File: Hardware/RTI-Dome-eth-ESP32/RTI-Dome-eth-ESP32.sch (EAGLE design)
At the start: 101 parts, among them IC1 REG1117FA-5.0_500, IC2 24LC64T-I/SN, IC8 REG1117-3.3V, J2 XT60PW-M, T1 MMBT3904LT1, T2 MMBT3904LT1, T3 MMBT3904LT1, U1 W5500, U2 ESP32-DevKitC ESP32-WROOM-32U, X9 J1011F01PNL

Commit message: Use switching regulator for the 5v. Can take from 8V to 40V in.
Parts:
- removed C2: 100uF, samacsys:MAL215099804E3""
- removed C27, C28, C3: 10uF, rcl:C-EUC0603
- removed IC1: REG1117FA-5.0_500, REG1117FA-5.0_500:REG1117FA-5.0_500
- removed X11: (no value), rti:AK500/2
- added C25, C26: 180uF, samacsys:EEE-FNE181XUP
- added C29, C30, C31: 15uF 50V, samacsys:865080643007
- added C7: 1nF, rcl:C-EUC0805
- added C8: 10nF, rcl:C-EUC0805
- added C9: 470nF, rcl:C-EUC1206
- added D2: VSSAF5L45-M3_6A, samacsys:VSSAF5L45-M3_6A
- added IC3: LM2679SD-5.0_NOPB, samacsys:LM2679SD-5.0_NOPB
- added L1: SRP1038CC-220M, samacsys:SRP1038CC-220M
- added R11: 5.6K, rcl:R-EU_R0603
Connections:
- new net 5V_SW: C8.1, D2.K, IC3.SWITCH_OUTPUT_1, IC3.SWITCH_OUTPUT_2, IC3.SWITCH_OUTPUT_3, L1.1
- new net CB: C8.2, IC3.CB
- new net N$1: IC3.CURRENT_ADJUST, R11.1
- new net N$4: C7.2, IC3.SS
- net +12V: now also C29.+, C30.+, C31.+, C9.2, IC3.INPUT_1, IC3.INPUT_2; no longer C2.+, C27.1, C3.1, IC1.VIN, X11-2.KL
- net GND: now also C25.-, C26.-, C29.-, C30.-, C31.-, C7.1, C9.1, D2.A, IC3.EP, IC3.GND, R11.2; no longer C2.-, C27.2, C28.2, C3.2, IC1.GND, X11-1.KL
- net VCC: now also C25.+, C26.+, IC3.FB, L1.2; no longer C28.1, IC1.VOUT_1, IC1.VOUT_2
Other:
- moved on the sheet: JP1, U2

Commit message: Switch IO port to Wurth ones.
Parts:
- removed R10, R2, R6, R7, R8: 100K 0.1%, rcl:R-EU_R0603
- removed X1, X12, X3, X8: (no value), rti:AK500/2
- removed X10, X2, X4, X5, X6, X7: (no value), rti:AK500/3
- added J1, J3, J4, J6, J7: 691313510003, samacsys:691313510003
- added J10, J11, J12, J8, J9: 691313510002, samacsys:691313510002
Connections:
- removed net N$2: R7.2, R8.1
- removed net N$3: R10.1, R8.2
- removed net N$5: R2.2, R7.1
- net +12V: now also J7.1; no longer R10.2, X5-1.KL
- net AT_PARK_PIN-IN_EXT: now also J11.2; no longer X12-2.KL
- net BUTTON_EAST_OPEN-IN_EXT: now also J6.2; no longer X4-2.KL
- net BUTTON_WEST_CLOSE-IN_EXT: now also J6.3; no longer X4-3.KL
- net DIR_5V_OUT: now also J3.2; no longer X10-2.KL
- net EN_5V_OUT: now also J4.2; no longer X2-2.KL
- net GND: now also J1.1, J11.1, J3.1, J4.1, J6.1, J7.3, J8.1, J9.1; no longer R6.1, X1-1.KL, X10-1.KL, X12-1.KL, X2-1.KL, X3-1.KL, X4-1.KL, X5-3.KL, X6-1.KL, X7-1.KL
- net HOME_SHUTTER_CLOSED-IN_EXT: now also J8.2; no longer X1-2.KL
- net RG-11-IN_EXT: now also J7.2; no longer X5-2.KL
- net SHUTTER_OPENED-IN_EXT: now also J9.2; no longer X3-2.KL
- net SPARE1-IN_EXT: now also J10.1; no longer X8-1.KL
- net SPARE2-IN_EXT: now also J10.2; no longer X8-2.KL
- net SPARE_OUT1_5V: now also J12.2; no longer X7-3.KL
- net SPARE_OUT2_5V: now also J12.1; no longer X7-2.KL
- net STEP_5V_OUT: now also J1.2; no longer X6-2.KL
- net VCC: now also J1.3, J3.3, J4.3; no longer X10-3.KL, X2-3.KL, X6-3.KL
- net VPIN: no longer R2.1, R6.2
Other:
- moved on the sheet: J2

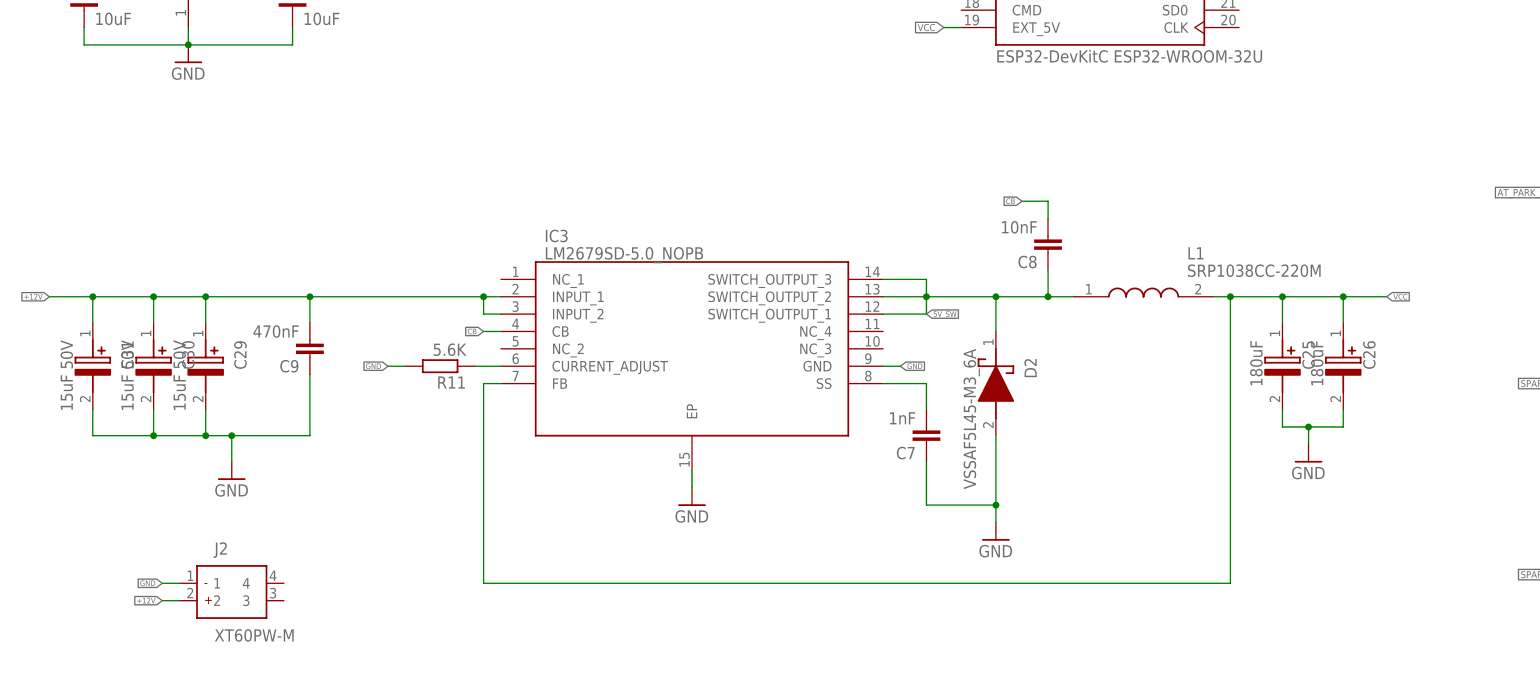
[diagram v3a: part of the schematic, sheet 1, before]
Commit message: Change the 5V regulator on the rotatyor esp32 board.
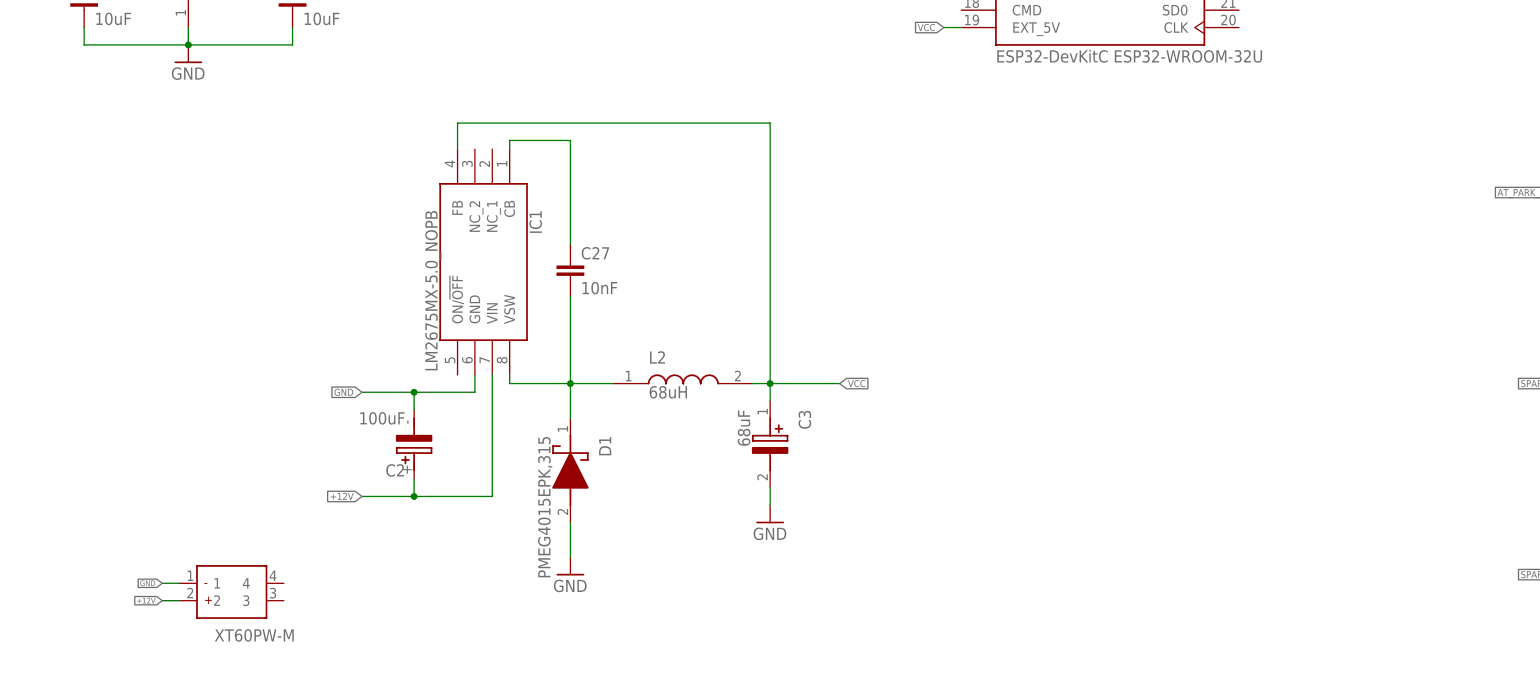
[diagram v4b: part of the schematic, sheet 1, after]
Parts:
- removed C25, C26: 180uF, samacsys:EEE-FNE181XUP
- removed C29, C30, C31: 15uF 50V, samacsys:865080643007
- removed C7: 1nF, rcl:C-EUC0805
- removed C8: 10nF, rcl:C-EUC0805
- removed C9: 470nF, rcl:C-EUC1206
- removed D2: VSSAF5L45-M3_6A, samacsys:VSSAF5L45-M3_6A
- removed IC3: LM2679SD-5.0_NOPB, samacsys:LM2679SD-5.0_NOPB
- removed L1: SRP1038CC-220M, samacsys:SRP1038CC-220M
- removed R11: 5.6K, rcl:R-EU_R0603
- added C2: 100uF, samacsys:MAL215099804E3""
- added C27: 10nF, rcl:C-EUC0805
- added C3: 68uF, samacsys:EEE-FP1C680AL
- added D1: PMEG4015EPK,315, samacsys:PMEG4015EPK,315
- added IC1: LM2675MX-5.0_NOPB, samacsys:LM2675MX-5.0_NOPB
- added L2: 68uH, samacsys:784777470
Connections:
- removed net 5V_SW: C8.1, D2.K, IC3.SWITCH_OUTPUT_1, IC3.SWITCH_OUTPUT_2, IC3.SWITCH_OUTPUT_3, L1.1
- removed net CB: C8.2, IC3.CB
- removed net N$1: IC3.CURRENT_ADJUST, R11.1
- removed net N$4: C7.2, IC3.SS
- new net N$2: C27.1, IC1.CB
- new net SWV: C27.2, D1.K, IC1.VSW, L2.1
- net +12V: now also C2.+, IC1.VIN; no longer C29.+, C30.+, C31.+, C9.2, IC3.INPUT_1, IC3.INPUT_2
- net GND: now also C2.-, C3.-, D1.A, IC1.GND; no longer C25.-, C26.-, C29.-, C30.-, C31.-, C7.1, C9.1, D2.A, IC3.EP, IC3.GND, R11.2
- net VCC: now also C3.+, IC1.FB, L2.2; no longer C25.+, C26.+, IC3.FB, L1.2

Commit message: Fix components orientation in the library to match JLCPCB
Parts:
- C2: MPN (none) -> C249838
- IC2: device Microchip_By_element14_Batch_1:24LC64T-I/SN -> rti:24LC64T-I/SN
- L2: value 68uH -> 47uH; MPN (none) -> 784777470
- R23: value 10 1% -> 10.0 1%; MPN RT0805FRE1310RL -> C881123
- U2: value ESP32-DevKitC ESP32-WROOM-32U -> ESP32-DevKitC-32UE
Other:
- moved on the sheet: C2, C27, C3, D1, IC1, L2

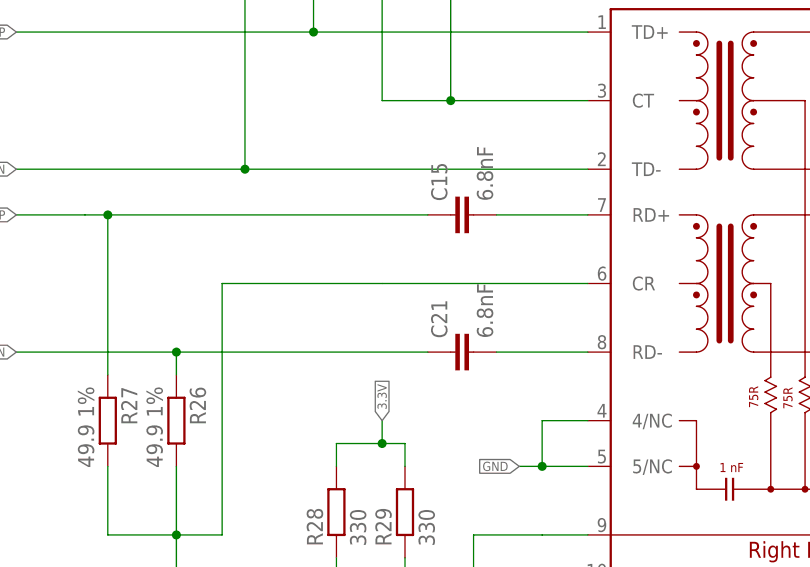
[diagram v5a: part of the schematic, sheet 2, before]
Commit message: Re-adding the domeClient.stop();
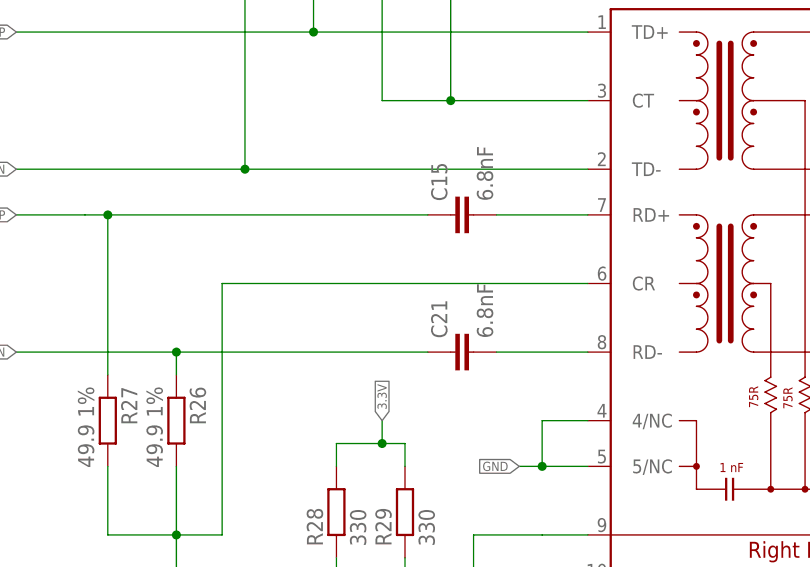
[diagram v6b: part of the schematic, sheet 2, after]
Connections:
- net N$10 renamed L_LED+
- net N$11 renamed RD+
- net N$12 renamed RD-
- net N$13 renamed CT
- net N$7 renamed CR
- net N$8 renamed R_LED+
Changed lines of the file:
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@@
 <part name="FRAME1" library="frames" library_urn="urn:adsk.eagle:library:229" deviceset="DINA3_L" device=""/>
 <part name="GND7" library="supply1" library_urn="urn:adsk.eagle:library:371" deviceset="GND" device=""/>
-<part name="U1" library="W5500" library_urn="urn:adsk.eagle:library:37501005" deviceset="W5500" device="" package3d_urn="urn:adsk.eagle:package:37501008/3" value="W5500">
+<part name="U1" library="W5500" library_urn="urn:adsk.eagle:library:37501005" deviceset="W5500" device="" package3d_urn="urn:adsk.eagle:package:37501008/4" value="W5500">
 <attribute name="MPN" value="W5500"/>
 </part>
@@
 <part name="GND16" library="supply1" library_urn="urn:adsk.eagle:library:371" deviceset="GND" device=""/>
 <part name="J2" library="samacsys" library_urn="urn:adsk.eagle:library:37256869" deviceset="XT60PW-M" device="" package3d_urn="urn:adsk.eagle:package:37256940/7"/>
-<part name="IC2" library="rti" library_urn="urn:adsk.eagle:library:37256580" deviceset="24LC64T-I/SN" device="" package3d_urn="urn:adsk.eagle:package:37894665/5"/>
+<part name="IC2" library="rti" library_urn="urn:adsk.eagle:library:37256580" deviceset="24LC64T-I/SN" device="" package3d_urn="urn:adsk.eagle:package:37894665/6"/>
 <part name="GND21" library="supply1" library_urn="urn:adsk.eagle:library:371" deviceset="GND" device=""/>
-<part name="IC8" library="burr-brown" library_urn="urn:adsk.eagle:library:37504555" deviceset="REG1117" device="" package3d_urn="urn:adsk.eagle:package:37504714/2" value="REG1117-3.3V">
+<part name="IC8" library="burr-brown" library_urn="urn:adsk.eagle:library:37504555" deviceset="REG1117" device="" package3d_urn="urn:adsk.eagle:package:37504714/3" value="REG1117-3.3V">
 <attribute name="MPN" value="REG1117-3.3/2K5"/>
 </part>
@@
 </part>
 <part name="GND38" library="supply1" library_urn="urn:adsk.eagle:library:371" deviceset="GND" device=""/>
-<part name="U$1" library="rti" library_urn="urn:adsk.eagle:library:37256580" deviceset="74*541" device="B" package3d_urn="urn:adsk.eagle:package:37318379/3" value="74HCT541PWR"/>
-<part name="U$3" library="rti" library_urn="urn:adsk.eagle:library:37256580" deviceset="74*541" device="B" package3d_urn="urn:adsk.eagle:package:37318379/3" value="74LVC541APWR"/>
-<part name="T1" library="samacsys" library_urn="urn:adsk.eagle:library:37256869" deviceset="MMBT3904LT1" device="" package3d_urn="urn:adsk.eagle:package:45494141/2"/>
-<part name="T2" library="samacsys" library_urn="urn:adsk.eagle:library:37256869" deviceset="MMBT3904LT1" device="" package3d_urn="urn:adsk.eagle:package:45494141/2"/>
-<part name="T3" library="samacsys" library_urn="urn:adsk.eagle:library:37256869" deviceset="MMBT3904LT1" device="" package3d_urn="urn:adsk.eagle:package:45494141/2"/>
+<part name="U$1" library="rti" library_urn="urn:adsk.eagle:library:37256580" deviceset="74*541" device="B" package3d_urn="urn:adsk.eagle:package:37318379/4" value="74HCT541PWR"/>
+<part name="U$3" library="rti" library_urn="urn:adsk.eagle:library:37256580" deviceset="74*541" device="B" package3d_urn="urn:adsk.eagle:package:37318379/4" value="74LVC541APWR"/>
+<part name="T1" library="samacsys" library_urn="urn:adsk.eagle:library:37256869" deviceset="MMBT3904LT1" device="" package3d_urn="urn:adsk.eagle:package:45494141/3"/>
+<part name="T2" library="samacsys" library_urn="urn:adsk.eagle:library:37256869" deviceset="MMBT3904LT1" device="" package3d_urn="urn:adsk.eagle:package:45494141/3"/>
+<part name="T3" library="samacsys" library_urn="urn:adsk.eagle:library:37256869" deviceset="MMBT3904LT1" device="" package3d_urn="urn:adsk.eagle:package:45494141/3"/>
 <part name="R12" library="rcl" library_urn="urn:adsk.eagle:library:334" deviceset="R-EU_" device="R0603" package3d_urn="urn:adsk.eagle:package:23555/3" value="1K">
 <spice>
@@
 <part name="J11" library="samacsys" library_urn="urn:adsk.eagle:library:37256869" deviceset="691313510002" device="" package3d_urn="urn:adsk.eagle:package:45454773/6"/>
 <part name="J12" library="samacsys" library_urn="urn:adsk.eagle:library:37256869" deviceset="691313510002" device="" package3d_urn="urn:adsk.eagle:package:45454773/6"/>
-<part name="IC1" library="samacsys" library_urn="urn:adsk.eagle:library:37256869" deviceset="LM2675MX-5.0_NOPB" device="" package3d_urn="urn:adsk.eagle:package:45493951/4"/>
+<part name="IC1" library="samacsys" library_urn="urn:adsk.eagle:library:37256869" deviceset="LM2675MX-5.0_NOPB" device="" package3d_urn="urn:adsk.eagle:package:45493951/5"/>
 <part name="D1" library="samacsys" library_urn="urn:adsk.eagle:library:37256869" deviceset="PMEG4015EPK,315" device="" package3d_urn="urn:adsk.eagle:package:45493982/4"/>
-<part name="C2" library="samacsys" library_urn="urn:adsk.eagle:library:37256869" deviceset="MAL215099804E3" device="&quot;&quot;" package3d_urn="urn:adsk.eagle:package:38013982/8" value="100uF">
+<part name="C2" library="samacsys" library_urn="urn:adsk.eagle:library:37256869" deviceset="MAL215099804E3" device="&quot;&quot;" package3d_urn="urn:adsk.eagle:package:38013982/9" value="100uF">
 <attribute name="MPN" value="C249838"/>
 </part>
-<part name="C3" library="samacsys" library_urn="urn:adsk.eagle:library:37256869" deviceset="EEE-FP1C680AL" device="" package3d_urn="urn:adsk.eagle:package:45493987/5" value="68uF"/>
+<part name="C3" library="samacsys" library_urn="urn:adsk.eagle:library:37256869" deviceset="EEE-FP1C680AL" device="" package3d_urn="urn:adsk.eagle:package:45493987/6" value="68uF"/>
 <part name="C27" library="rcl" library_urn="urn:adsk.eagle:library:334" deviceset="C-EU" device="C0805" package3d_urn="urn:adsk.eagle:package:23617/2" value="10nF"/>
-<part name="L2" library="samacsys" library_urn="urn:adsk.eagle:library:37256869" deviceset="784777470" device="" package3d_urn="urn:adsk.eagle:package:45494005/4" value="47uH">
+<part name="L2" library="samacsys" library_urn="urn:adsk.eagle:library:37256869" deviceset="784777470" device="" package3d_urn="urn:adsk.eagle:package:45494005/5" value="47uH">
 <attribute name="MPN" value="784777470"/>
 </part>
@@
 </segment>
 </net>
-<net name="N$7" class="3">
+<net name="CR" class="3">
 <segment>
 <pinref part="X9" gate="G$1" pin="CR"/>
-<wire x1="309.88" y1="193.04" x2="287.02" y2="193.04" width="0.1524" layer="91"/>
-<wire x1="287.02" y1="193.04" x2="269.24" y2="193.04" width="0.1524" layer="91"/>
+<wire x1="309.88" y1="193.04" x2="269.24" y2="193.04" width="0.1524" layer="91"/>
 <wire x1="269.24" y1="193.04" x2="269.24" y2="165.1" width="0.1524" layer="91"/>
 <pinref part="R27" gate="G$1" pin="2"/>
@@
 </segment>
 </net>
-<net name="N$8" class="0">
+<net name="R_LED+" class="0">
 <segment>
 <pinref part="X9" gate="G$1" pin="A-R"/>
@@
 </segment>
 </net>
-<net name="N$10" class="0">
+<net name="L_LED+" class="0">
 <segment>
 <pinref part="X9" gate="G$1" pin="AL"/>
@@
 </segment>
 </net>
-<net name="N$11" class="0">
+<net name="RD+" class="0">
 <segment>
 <pinref part="X9" gate="G$1" pin="RD+"/>
@@
 </segment>
 </net>
-<net name="N$12" class="0">
+<net name="RD-" class="0">
 <segment>
 <pinref part="X9" gate="G$1" pin="RD-"/>
@@
 </segment>
 </net>
-<net name="N$13" class="3">
+<net name="CT" class="3">
 <segment>
 <pinref part="R23" gate="G$1" pin="1"/>
